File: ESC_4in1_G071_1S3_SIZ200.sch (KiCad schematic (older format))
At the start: 61 parts, among them J1 Conn_01x08, U1 STM32G071GBU6, U10 NCP81253MNTBG, U11 SIZ200DT-T1-GE3, U12 NCP81253MNTBG, U13 SIZ200DT-T1-GE3, U14 TPS630701, U15 TPS727xxDSE, U16 INA185, U2 NCP81253MNTBG, U3 SIZ200DT-T1-GE3, U4 NCP81253MNTBG, U5 SIZ200DT-T1-GE3, U6 NCP81253MNTBG, U7 SIZ200DT-T1-GE3, U8 NCP81253MNTBG, U9 SIZ200DT-T1-GE3

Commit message: update schematic
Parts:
- added C22, C23, C24, C25, C26, C27, C28, C29, C30, C31, C32, C33, C34, C35, C36: 100n, Capacitor_SMD:C_0402_1005Metric, symbol Device:C_Small
- added R10, R11, R12, R13, R14, R15, R16, R17, R18, R3, R4, R5, R6, R7, R8, R9: 4k7, Capacitor_SMD:C_0402_1005Metric, symbol Device:R_Small
- added RN10, RN15, RN21, RN8: 10k, 11_PSoC_FC_whoop:R_Array_Convex_2x0402_dense, symbol Device:R_Pack02
- added RN11, RN17, RN23, RN7: 2k2, 11_PSoC_FC_whoop:R_Array_Convex_2x0402_dense, symbol Device:R_Pack02
- added RN12, RN18, RN24, RN9: 2k2, 11_PSoC_FC_whoop:R_Array_Convex_4x0402_dense, symbol Device:R_Pack04
- added RN13, RN14, RN16, RN19, RN20, RN22: 10R0, 11_PSoC_FC_whoop:R_Array_Convex_2x0402_dense, symbol Device:R_Pack02
- added TP10, TP11, TP12, TP13, TP14, TP9: TestPoint_Flag, 11_PSoC_FC_whoop:esc_pad, symbol Connector:TestPoint_Flag
- added U17, U21, U28: STM32G071GBU6, UFQPFN28:UFQFPN28, symbol STM32G071:STM32G071GBU6
- added U18, U20, U23, U25, U27, U30: NCP81161MNTBG, 11_PSoC_FC_whoop:DFN-8-1EP_2x2mm_P0.5mm_EP0.9x1.3mm_narrow, symbol lib_ultimateFC:NCP81253MNTBG
- added U19, U22, U24, U26, U29, U31: SIZ200DT-T1-GE3, 11_PSoC_FC_whoop:PowerPAIR3.3x3.3, symbol lib_ultimateFC:SIZ322DT-T1-GE3
- RN1, RN2, RN3, RN4, RN5, RN6: footprint Resistor_SMD:R_Array_Convex_2x0402 -> 11_PSoC_FC_whoop:R_Array_Convex_2x0402_dense
- U10, U12, U2, U4, U6, U8: value NCP81253MNTBG -> NCP81161MNTBG
- U15: value TPS727xxDSE -> TPS72733DSE
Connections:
- net labels added: ESC1_SWDCLK, ESC1_SWDIO, ESC2_IN, ESC2_MA, ESC2_MB, ESC2_MC, ESC2_SWDCLK, ESC2_SWDIO, ESC2_Y, ESC3_A, ESC3_A_EN, ESC3_A_PWM, ESC3_B, ESC3_B_EN, ESC3_B_PWM, ESC3_C, ESC3_C_EN, ESC3_C_PWM, ESC3_IN, ESC3_MA, ESC3_MB, ESC3_MC, ESC3_SWDCLK, ESC3_SWDIO, ESC3_Y, ESC4_A, ESC4_A_EN, ESC4_A_PWM, ESC4_B, ESC4_B_EN, ESC4_B_PWM, ESC4_C, ESC4_C_EN, ESC4_C_PWM, ESC4_IN, ESC4_MA, ESC4_MB, ESC4_MC, ESC4_SWDCLK, ESC4_SWDIO, ESC4_Y, ESCx_tele
- net labels removed: SWDCLK, SWDIO
- wire segments 289 -> 693
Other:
- note added: "1"
- note added: "2"
- note added: "3"
- note added: "4"
- note added: "ESC1"
- note added: "ESC2"
- note added: "ESC3"
- note added: "ESC4"
- note added: "PWM signals are open drain with 5V pull-up\nEN are push-pull"
- moved on the sheet: C1, C10, C11, C12, C2, C20, C21, C3, C4, C5, C6, C7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

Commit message: - ESC1 pinout updated - ESC1 schematic done - ESC1 routed - increased PCB size to 26*27 mm
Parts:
- added TP15, TP16, TP17, TP18, TP19, TP20, TP21, TP22: TestPoint, 11_PSoC_FC_whoop:TestPoint_Pad_D1.0mm_dense, symbol Connector:TestPoint
- R10, R11, R12, R13, R14, R15, R16, R17, R18, R2, R3, R4, R5, R6, R7, R8, R9: footprint Capacitor_SMD:C_0402_1005Metric -> Resistor_SMD:R_0402_1005Metric
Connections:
- net labels added: ESC1_A_DRVH, ESC1_A_DRVL, ESC1_A_GH, ESC1_A_GL, ESC1_B_DRVH, ESC1_B_DRVL, ESC1_B_GH, ESC1_B_GL, ESC1_C_DRVH, ESC1_C_DRVL, ESC1_C_GH, ESC1_C_GL, ESC2_A_DRVH, ESC2_A_DRVL, ESC2_A_GH, ESC2_A_GL, ESC2_B_DRVH, ESC2_B_DRVL, ESC2_B_GH, ESC2_B_GL, ESC2_C_DRVH, ESC2_C_DRVL, ESC2_C_GH, ESC2_C_GL, ESC3_A_DRVH, ESC3_A_DRVL, ESC3_A_GH, ESC3_A_GL, ESC3_B_DRVH, ESC3_B_DRVL, ESC3_B_GH, ESC3_B_GL, ESC3_C_DRVH, ESC3_C_DRVL, ESC3_C_GH, ESC3_C_GL, ESC4_A_DRVH, ESC4_A_DRVL, ESC4_A_GH, ESC4_A_GL, ESC4_B_DRVH, ESC4_B_DRVL, ESC4_B_GH, ESC4_B_GL, ESC4_C_DRVH, ESC4_C_DRVL, ESC4_C_GH, ESC4_C_GL
- wire segments 693 -> 630
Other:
- moved on the sheet: RN1, RN11, RN12, RN13, RN14, RN16, RN17, RN18, RN19, RN2, RN20, RN22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

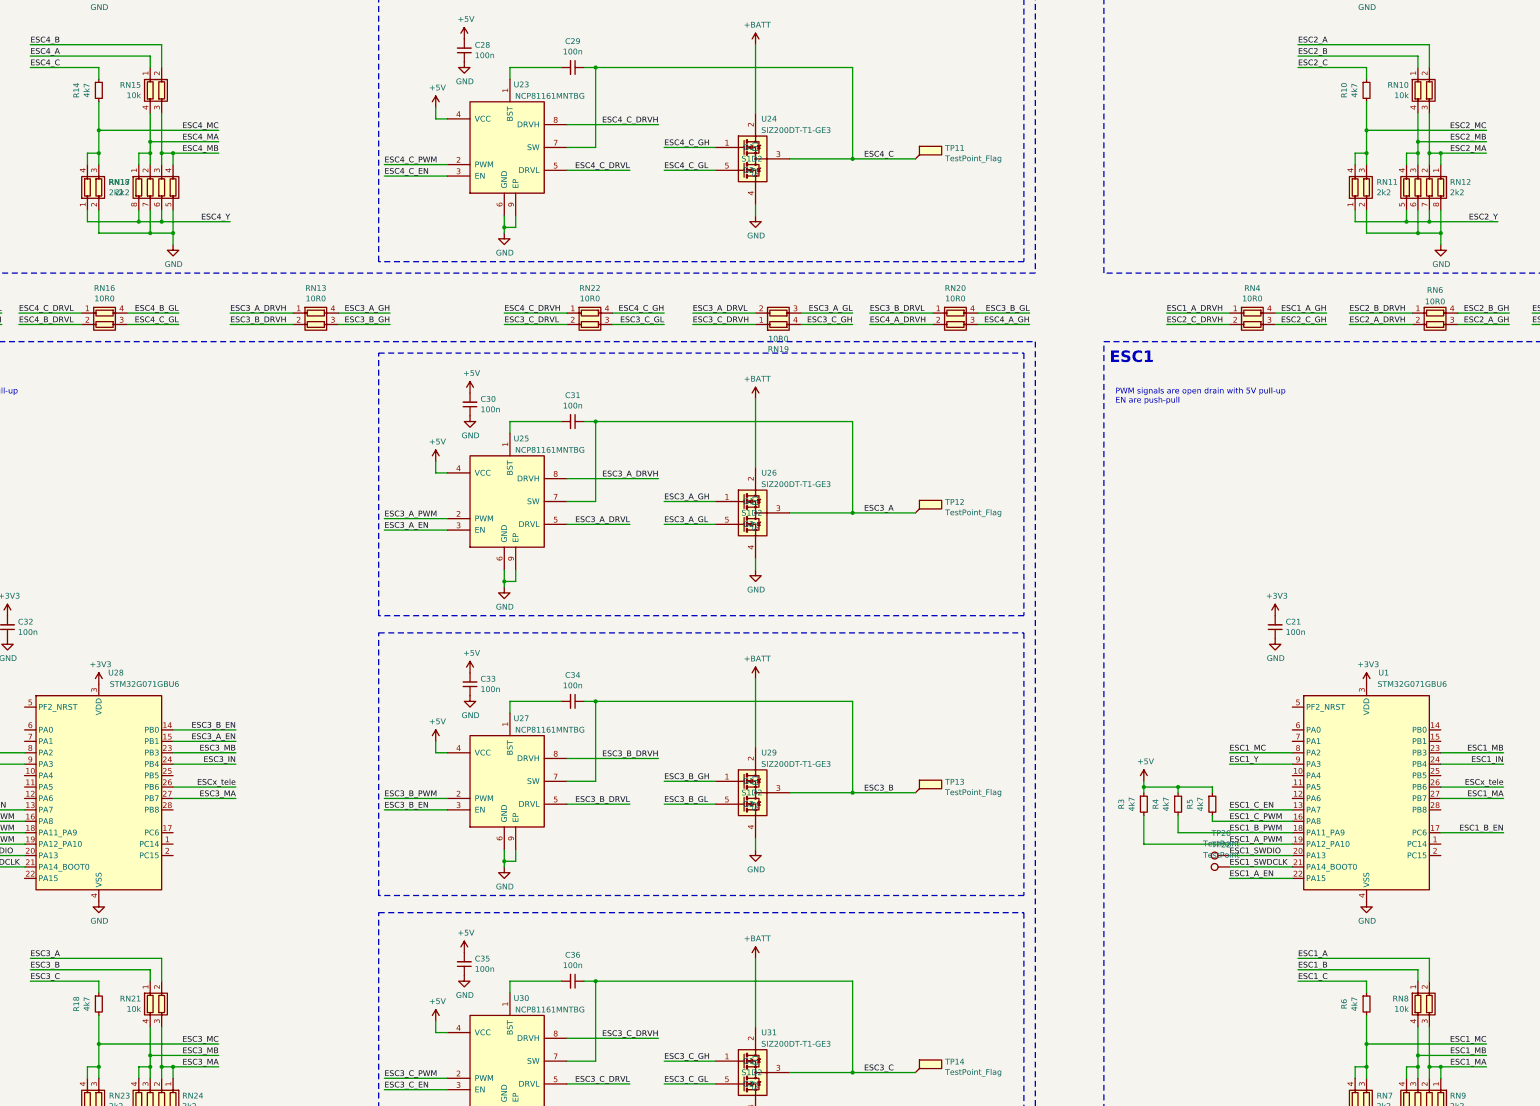
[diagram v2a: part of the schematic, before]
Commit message: update schematic and layout
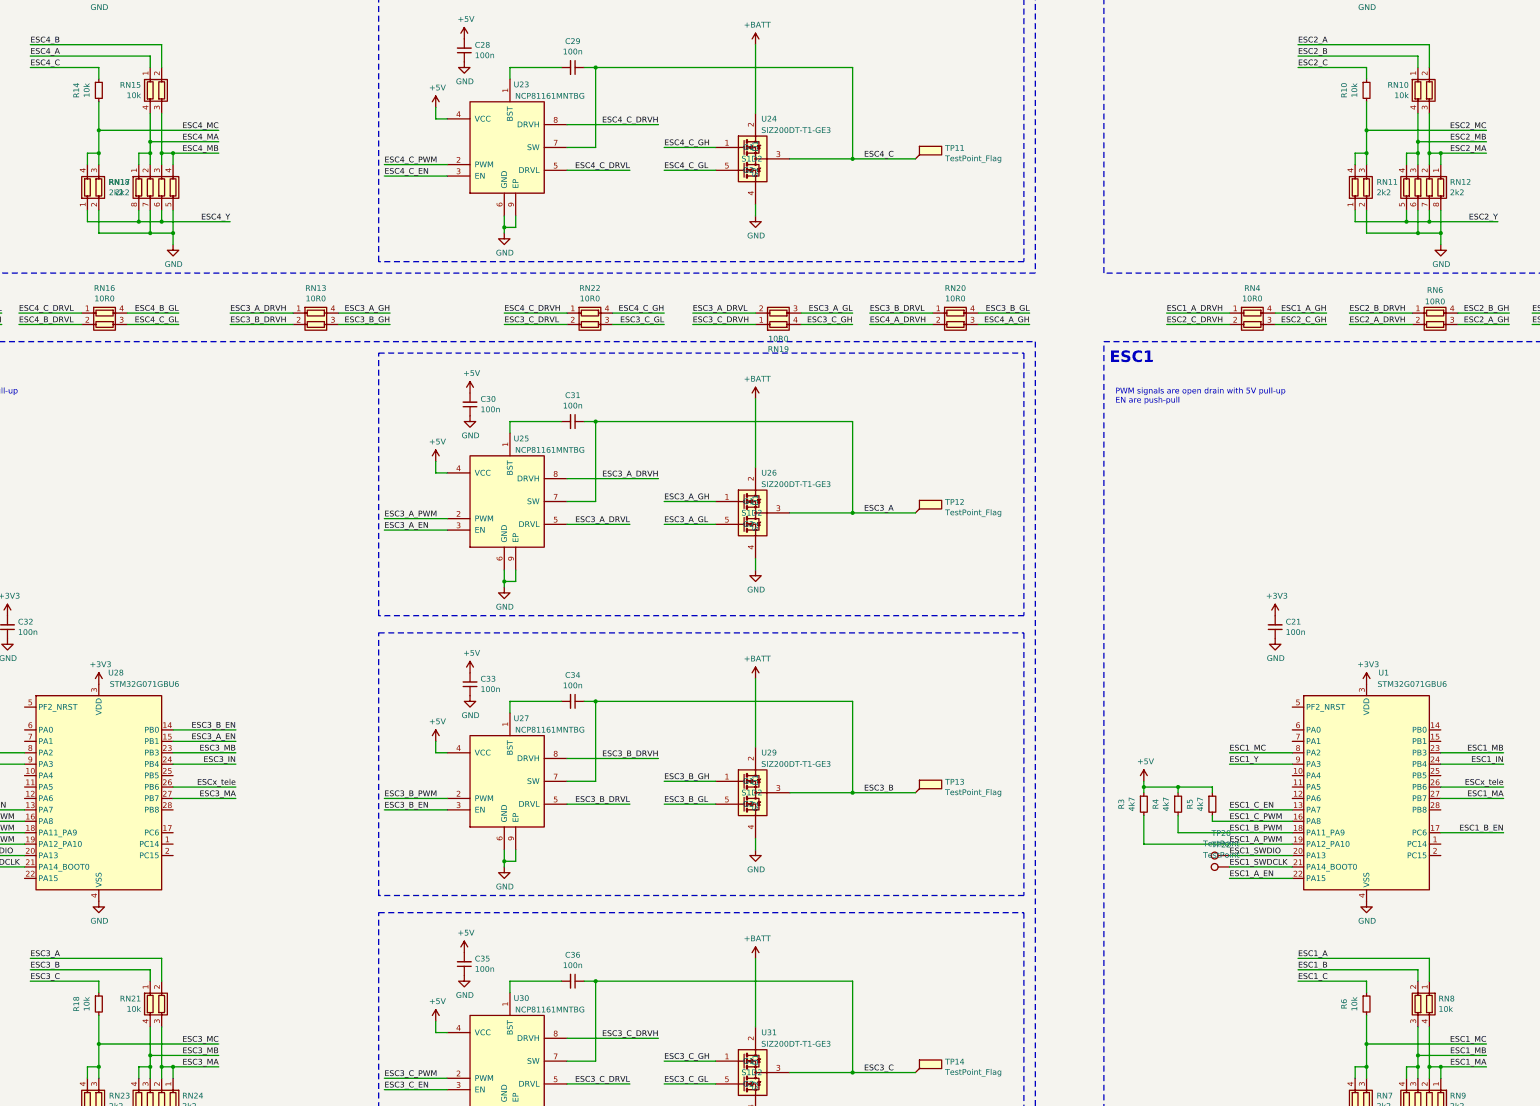
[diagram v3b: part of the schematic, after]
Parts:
- R10, R14, R18, R6: value 4k7 -> 10k
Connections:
- net ESC1_A: now also RN8.1 (R1.1); no longer RN8.2 (R2.1)
- net ESC1_B: now also RN8.2 (R2.1); no longer RN8.1 (R1.1)
- net ESC1_MA: now also RN8.4 (R1.2); no longer RN8.3 (R2.2)
- net ESC1_MB: now also RN8.3 (R2.2); no longer RN8.4 (R1.2)
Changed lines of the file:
@@
 L Device:R_Pack02 RN8
 U 1 1 6020298A
-P 24050 18350
-F 0 "RN8" H 23870 18304 50  0000 R CNN
-F 1 "10k" H 23870 18395 50  0000 R CNN
-F 2 "11_PSoC_FC_whoop:R_Array_Convex_2x0402_dense" V 24325 18350 50  0001 C CNN
-F 3 "~" H 24050 18350 50  0001 C CNN
-	1    24050 18350
-	1    0    0    1
+P 23950 18350
+F 0 "RN8" H 23770 18304 50  0000 R CNN
+F 1 "10k" H 23770 18395 50  0000 R CNN
+F 2 "11_PSoC_FC_whoop:R_Array_Convex_2x0402_dense" V 24225 18350 50  0001 C CNN
+F 3 "~" H 23950 18350 50  0001 C CNN
+	1    23950 18350
+	-1   0    0    1
 $EndComp
 $Comp
@@
 P 23500 18350
 F 0 "R6" V 23304 18350 50  0000 C CNN
-F 1 "4k7" V 23395 18350 50  0000 C CNN
+F 1 "10k" V 23395 18350 50  0000 C CNN
 F 2 "Resistor_SMD:R_0402_1005Metric" H 23500 18350 50  0001 C CNN
 F 3 "~" H 23500 18350 50  0001 C CNN
@@
 P 23500 10350
 F 0 "R10" V 23304 10350 50  0000 C CNN
-F 1 "4k7" V 23395 10350 50  0000 C CNN
+F 1 "10k" V 23395 10350 50  0000 C CNN
 F 2 "Resistor_SMD:R_0402_1005Metric" H 23500 10350 50  0001 C CNN
 F 3 "~" H 23500 10350 50  0001 C CNN
@@
 P 12400 18350
 F 0 "R18" V 12204 18350 50  0000 C CNN
-F 1 "4k7" V 12295 18350 50  0000 C CNN
+F 1 "10k" V 12295 18350 50  0000 C CNN
 F 2 "Resistor_SMD:R_0402_1005Metric" H 12400 18350 50  0001 C CNN
 F 3 "~" H 12400 18350 50  0001 C CNN
@@
 P 12400 10350
 F 0 "R14" V 12204 10350 50  0000 C CNN
-F 1 "4k7" V 12295 10350 50  0000 C CNN
+F 1 "10k" V 12295 10350 50  0000 C CNN
 F 2 "Resistor_SMD:R_0402_1005Metric" H 12400 10350 50  0001 C CNN
 F 3 "~" H 12400 10350 50  0001 C CNN

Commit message: update schematic and layout
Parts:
- added C37, C38, C39, C40, C41, C42, C43, C44, C45, C46, C47, C48, C49, C50, C51, C52, C53, C54, C55, C56: 22u, 11_PSoC_FC_whoop:C_0805_2012Metric_dense, symbol Device:C_Small
- added C57: 10u, Capacitor_SMD:C_0402_1005Metric, symbol Device:C_Small
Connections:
- net +5V: now also C57.2
- net +BATT: now also C37.2, C38.2, C39.2, C40.2, C41.2, C42.2, C43.2, C44.2, C45.2, C46.2, C47.2, C48.2, C49.2, C50.2, C51.2, C52.2, C53.2, C54.2, C55.2, C56.2
- net ESC1_IN: now also J1.5 (Pin_5); no longer J1.3 (Pin_3)
- net ESC2_A: now also RN10.1 (R1.1); no longer RN10.2 (R2.1)
- net ESC2_A_DRVH: now also RN5.1 (R1.1); no longer RN6.2 (R2.1)
- net ESC2_A_DRVL: now also RN4.2 (R2.1); no longer RN1.1 (R1.1)
- net ESC2_A_EN: now also U17.22 (PA15); no longer U17.15 (PB1)
- net ESC2_A_GH: now also RN5.4 (R1.2); no longer RN6.3 (R2.2)
- net ESC2_A_GL: now also RN4.3 (R2.2); no longer RN1.4 (R1.2)
- net ESC2_B: now also RN10.2 (R2.1); no longer RN10.1 (R1.1)
- net ESC2_B_DRVH: now also RN5.2 (R2.1); no longer RN6.1 (R1.1)
- net ESC2_B_DRVL: now also RN6.1 (R1.1)
- net ESC2_B_EN: now also U17.17 (PC6); no longer U17.14 (PB0)
- net ESC2_B_GH: now also RN5.3 (R2.2); no longer RN6.4 (R1.2)
- net ESC2_B_GL: now also RN6.4 (R1.2)
- net ESC2_C_DRVH: now also RN6.2 (R2.1); no longer RN4.2 (R2.1)
- net ESC2_C_DRVL: now also RN1.1 (R1.1)
- net ESC2_C_GH: now also RN6.3 (R2.2); no longer RN4.3 (R2.2)
- net ESC2_C_GL: now also RN1.4 (R1.2)
- net ESC2_IN: now also J1.6 (Pin_6); no longer J1.4 (Pin_4)
- net ESC2_MA: now also RN10.4 (R1.2); no longer RN10.3 (R2.2)
- net ESC2_MB: now also RN10.3 (R2.2); no longer RN10.4 (R1.2)
- net ESC2_Y: now also RN12.6 (R3.2), RN12.8 (R1.2); no longer RN12.5 (R4.2), RN12.7 (R2.2)
- net ESC3_A: now also RN21.1 (R1.1); no longer RN21.2 (R2.1)
- net ESC3_A_EN: now also U28.22 (PA15); no longer U28.15 (PB1)
- net ESC3_B: now also RN21.2 (R2.1); no longer RN21.1 (R1.1)
- net ESC3_B_EN: now also U28.17 (PC6); no longer U28.14 (PB0)
- net ESC3_IN: now also J1.7 (Pin_7); no longer J1.5 (Pin_5)
- net ESC3_MA: now also RN21.4 (R1.2); no longer RN21.3 (R2.2)
- net ESC3_MB: now also RN21.3 (R2.2); no longer RN21.4 (R1.2)
- net ESC4_A_EN: now also U21.22 (PA15); no longer U21.15 (PB1)
- net ESC4_B_EN: now also U21.17 (PC6); no longer U21.14 (PB0)
- net ESC4_IN: now also J1.8 (Pin_8); no longer J1.6 (Pin_6)
- net ESCx_tele: now also J1.4 (Pin_4); no longer J1.8 (Pin_8)
- net GND: now also RN12.5 (R4.2), RN12.7 (R2.2), C37.1, C38.1, C39.1, C40.1, C41.1, C42.1, C43.1, C44.1, C45.1, C46.1, C47.1, C48.1, C49.1, C50.1, C51.1, C52.1, C53.1, C54.1, C55.1, C56.1, C57.1; no longer RN12.6 (R3.2), RN12.8 (R1.2)
- net IBat: now also J1.3 (Pin_3); no longer J1.7 (Pin_7)
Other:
- moved on the sheet: RN5

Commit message: update schematic and layout
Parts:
- removed J1: Conn_01x08, Connector_JST:JST_SH_SM08B-SRSS-TB_1x08-1MP_P1.00mm_Horizontal, symbol Connector_Generic:Conn_01x08
- added C58, C59, C60, C61, C62, C64, C65, C66, C67, C68, C69: 10u, Capacitor_SMD:C_0402_1005Metric, symbol Device:C_Small
- added C63: 100n, Capacitor_SMD:C_0402_1005Metric, symbol Device:C_Small
- added J1: Conn_01x10, 11_PSoC_FC_whoop:JST_SHL_SM10B-SHLS-TF_1x10-1MP_P1.00mm_Horizontal_dense, symbol Connector_Generic:Conn_01x10
- R1: value R_Shunt -> 0m5; footprint Resistor_SMD:R_Shunt_Vishay_WSKW0612 -> Resistor_SMD:R_1206_3216Metric; symbol Device:R_Shunt -> Device:R_Small
- U16: value INA185 -> INA186A2; footprint Package_TO_SOT_SMD:SOT-563 -> Package_TO_SOT_SMD:SOT-363_SC-70-6
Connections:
- net +3V3: now also C63.2
- net +5V: now also C58.2, C59.2, C60.2, C61.2, C62.2, C64.2, C65.2, C66.2, C67.2, C68.2, C69.2, J1.9 (Pin_9)
- net +BATT: now also J1.2 (Pin_2)
- net ESC1_IN: now also J1.5 (Pin_5)
- net ESC2_IN: now also J1.6 (Pin_6)
- net ESC3_IN: now also J1.7 (Pin_7)
- net ESC4_IN: now also J1.8 (Pin_8)
- net ESCx_tele: now also J1.4 (Pin_4)
- net GND: now also U16.4 (+), C58.1, C59.1, C60.1, C61.1, C62.1, C63.1, C64.1, C65.1, C66.1, C67.1, C68.1, C69.1, J1.1 (Pin_1), J1.10 (Pin_10)
- net IBat: now also J1.3 (Pin_3)
- net at R1.2: now also TP8.1, U16.5 (-); no longer U16.4 (+)
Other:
- moved on the sheet: C13, C14, C15, C16, C17, C18, C19, C20, C37, C38, C39, C40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

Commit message: update design files
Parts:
- removed RN13, RN16, RN2, RN5: 10R0, 11_PSoC_FC_whoop:R_Array_Convex_2x0402_dense, symbol Device:R_Pack02
- added R19, R20, R21, R22, R23, R24, R25, R26: 10R0, Resistor_SMD:R_0402_1005Metric, symbol Device:R
- added R27, R28, R29, R30: 1k, Resistor_SMD:R_0402_1005Metric, symbol Device:R_Small
- added RN2: 1k, 11_PSoC_FC_whoop:R_Array_Convex_4x0402_dense, symbol Device:R_Pack04
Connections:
- net ESC1_B_DRVL: now also R26.2
- net ESC1_B_GL: now also R26.1
- net ESC1_C_DRVL: now also R22.2
- net ESC1_C_GL: now also R22.1
- net ESC1_IN: now also RN2.1 (R1.1); no longer J1.5 (Pin_5)
- net ESC1_Y: now also RN9.6 (R3.2), RN9.8 (R1.2); no longer RN9.5 (R4.2), RN9.7 (R2.2)
- net ESC2_A_DRVH: now also R19.2
- net ESC2_A_GH: now also R19.1
- net ESC2_B_DRVH: now also R23.2
- net ESC2_B_GH: now also R23.1
- net ESC2_IN: now also RN2.2 (R2.1); no longer J1.6 (Pin_6)
- net ESC3_A_DRVH: now also R21.2
- net ESC3_A_GH: now also R21.1
- net ESC3_B_DRVH: now also R25.2
- net ESC3_B_GH: now also R25.1
- net ESC3_IN: now also RN2.3 (R3.1); no longer J1.7 (Pin_7)
- net ESC3_Y: now also RN24.6 (R3.2), RN24.8 (R1.2); no longer RN24.5 (R4.2), RN24.7 (R2.2)
- net ESC4_B_DRVL: now also R24.2
- net ESC4_B_GL: now also R20.1
- net ESC4_C_DRVL: now also R20.2
- net ESC4_C_GL: now also R24.1
- net ESC4_IN: now also RN2.4 (R4.1); no longer J1.8 (Pin_8)
- net ESCx_tele: now also R27.1, R28.1, R29.1, R30.1; no longer U1.26 (PB6), U17.26 (PB6), U21.26 (PB6), U28.26 (PB6)
- net GND: now also RN24.5 (R4.2), RN24.7 (R2.2), RN9.5 (R4.2), RN9.7 (R2.2); no longer RN24.6 (R3.2), RN24.8 (R1.2), RN9.6 (R3.2), RN9.8 (R1.2)
- new net: R30.2, U1.26 (PB6)
- new net: J1.8 (Pin_8), RN2.5 (R4.2)
- new net: J1.7 (Pin_7), RN2.6 (R3.2)
- new net: J1.6 (Pin_6), RN2.7 (R2.2)
- new net: J1.5 (Pin_5), RN2.8 (R1.2)
- new net: R28.2, U17.26 (PB6)
- new net: R29.2, U28.26 (PB6)
- new net: R27.2, U21.26 (PB6)
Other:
- note added: "Input: 1-3S (3...12.6 V)"
- moved on the sheet: C1, C2, C21, C3, C30, C31, C32, C33, C34, C35, C36, C4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
